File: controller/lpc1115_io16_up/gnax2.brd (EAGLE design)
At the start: 44.5 x 44 mm, 77 parts, among them J2 CON_10-1.27THT, SW1 SWITCH_X, T1 BC547C, T2 BC807-40, U1 DMHC4035LSD, U2 SN74AUP1T32, U3 BD9G101G, U4 LPC1115FBD48/303, U5 M25P10, X1 12MHz, X3 FIDUCIAL_0.6-1.2MM, X8 FIDUCIAL_0.6-1.2MM, X9 FIDUCIAL_0.6-1.2MM

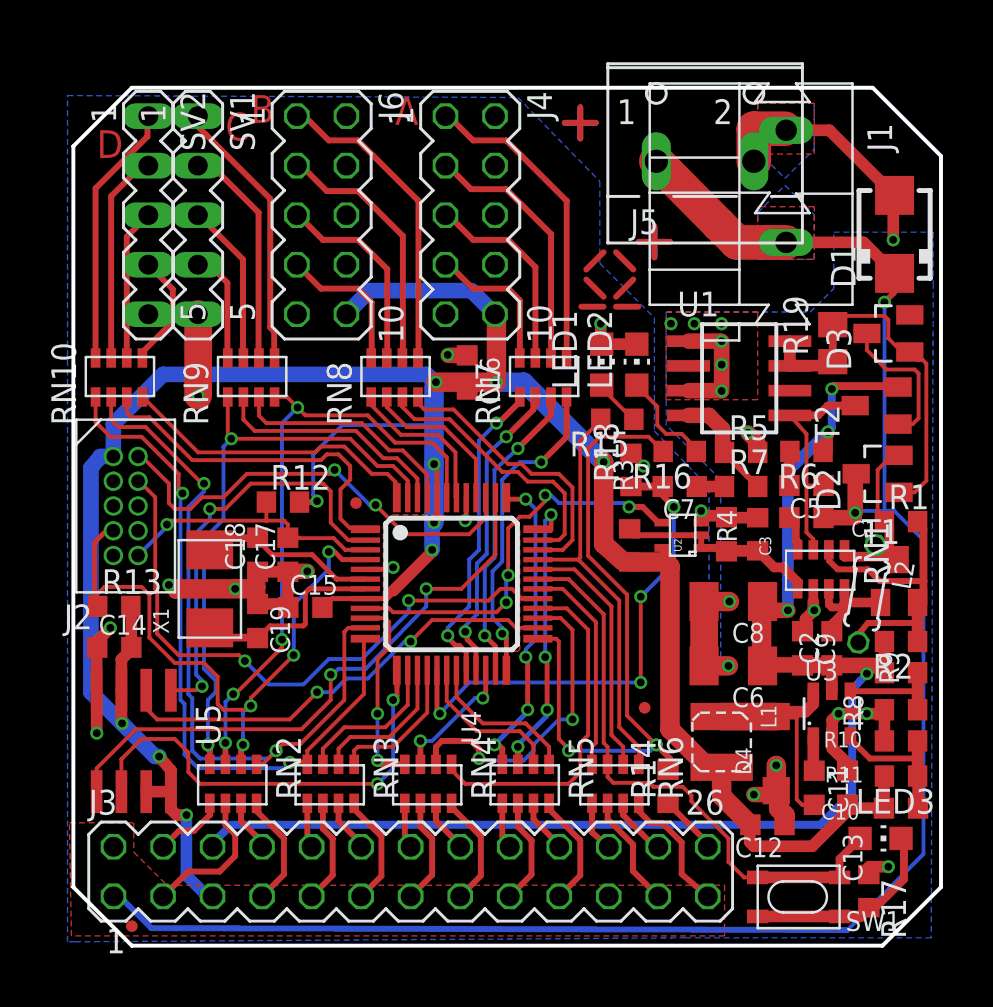
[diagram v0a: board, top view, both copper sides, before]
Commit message: current limiter for transmitter, change prog led behaviour, fix clamp layout
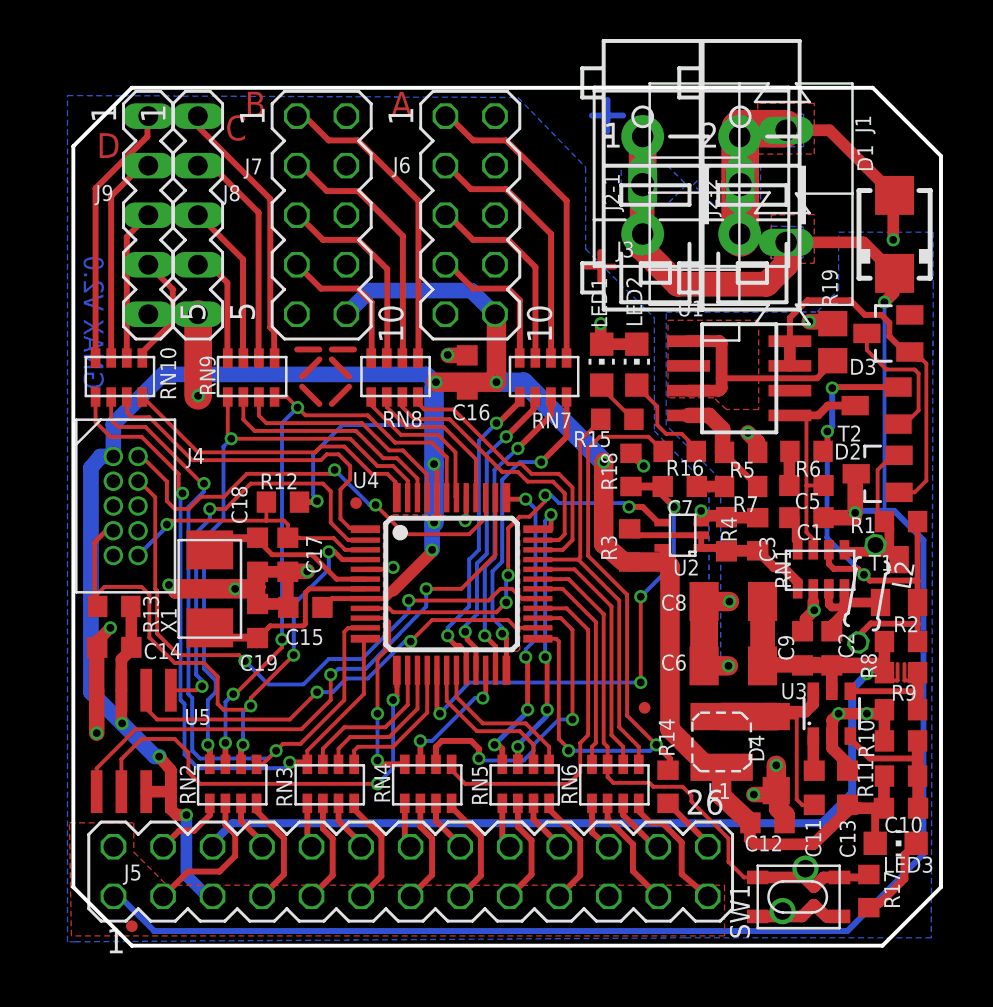
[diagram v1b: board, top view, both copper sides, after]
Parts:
- removed J2: CON_10-1.27THT, 000_ga:CON2X5_127-THT
- added J2-1, J2-2: (no value), con-wago:236-4XX
- added J7: (no value), con-lstb:MA05-2
- C3: value 330p -> 150p
- D3: value 8V2 -> 6V8
- J3: device con-lstb:MA13-2 -> 000_ga:W237-102
- J4: value (none) -> CON_10-1.27THT; device con-lstb:MA05-2 -> 000_ga:CON2X5_127-THT
- J5: device 000_ga:W237-102 -> con-lstb:MA13-2
- R19: value 3R3 -> 2R2
- SW1: value SWITCH_X -> (none)
- moved J5 40.6 mm to (17.3, 3.80)
- moved J3 39.2 mm to (31.7, 40.3)
- moved J4 23.6 mm to (2.05, 22.6)
- moved U$1 15.4 mm to (13.0, 29.0), turned to 180 degrees
- moved J6 7.62 mm to (20.4, 37.5)
- moved LED3 0.81 mm to (42.2, 5.25)
- moved C12 0.10 mm to (35.6, 6.30)
- moved R19 0.05 mm to (39.0, 30.9)
- renumbered SV1 to J8, SV2 to J9
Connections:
- removed net N$40: LED3.C, R17.2, SW1.3, SW1.4
- new net FX: R19.1, U1.1, U1.3
- new net N$46: L2.2, R1.2, R2.1, R6.1, RN1.2, T1.2, T2.E
- net EIB+: now also J2-1.1@1, J2-1.1@2
- net EIB_DC: now also J5.6; no longer J3.6, R6.1, T2.E
- net GND: now also J2-2.1@2, J5.21, J7.2, J7.4, J7.6, J7.8, J7.9, R19.2, SW1.3, SW1.4; no longer J2.9, J3.21, J4.2, J4.4, J4.6, J4.8, R17.1, U1.1, U1.3
- net N$1: no longer R19.1, R19.2
- net N$10: now also J6.5; no longer J4.5
- net N$11: now also J6.3; no longer J4.3
- net N$13: now also J6.1; no longer J4.1
- net N$16: now also J7.5; no longer J6.5
- net N$17: now also J7.3; no longer J6.3
- net N$22: now also J7.7; no longer J6.7
- net N$23: now also J7.1; no longer J6.1
- net N$25: now also LED3.C, R17.2; no longer L2.2, R1.2, R2.1, RN1.2, T1.2
- net N$38: now also J5.3; no longer J3.3
- net N$41: now also J5.7; no longer J3.7
- net N$42: now also J5.9; no longer J3.9
- net N$43: now also J5.11; no longer J3.11
- net N$44: now also J5.13; no longer J3.13
- net N$45: now also J5.4; no longer J3.4
- net N$47: now also J5.8; no longer J3.8
- net N$48: now also J5.10; no longer J3.10
- net N$49: now also J5.12; no longer J3.12
- net N$5: now also J6.7; no longer J4.7
- net N$50: now also J5.14; no longer J3.14
- net N$58: now also J5.15; no longer J3.15
- net N$59: now also J5.17; no longer J3.17
- net N$60: now also J5.16; no longer J3.16
- net N$61: now also J5.18; no longer J3.18
- net N$63: now also J5.19; no longer J3.19
- net N$64: now also J5.20; no longer J3.20
- net N$65: now also J5.22; no longer J3.22
- net N$66: now also J5.23; no longer J3.23
- net N$67: now also J5.24; no longer J3.24
- net N$68: now also J5.25; no longer J3.25
- net N$69: now also J5.26; no longer J3.26
- net RESET: now also J4.10; no longer J2.10
- net SWCLK: now also J4.4; no longer J2.4
- net SWDIO: now also J4.2; no longer J2.2
- net VCC: now also J4.1, J5.5, J7.10, LED3.A; no longer J2.1, J3.5, J4.10
- net XIO23: now also R17.1; no longer LED3.A
- net XIO8/ISP_EN: now also J4.7; no longer J2.7
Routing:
- net N$46: track 0.00 -> 30.4 mm, vias 0 -> 3
- net EIB_DC: track 74.6 -> 57.6 mm, vias 4 -> 1
- net FX: track 0.00 -> 11.9 mm
- net N$25: track 16.3 -> 4.46 mm
- net N$40: track 10.9 -> 0.00 mm
- net GND: track 80.8 -> 89.3 mm, vias 28 -> 23
- net EIB+: track 95.1 -> 102.6 mm
- net VCC: track 141.3 -> 145.1 mm
- net DUMMY3: track 3.20 -> 0.00 mm
- net DUMMY2: track 3.20 -> 0.00 mm
- net N$20: track 5.39 -> 7.31 mm
- net N$12: track 11.8 -> 12.3 mm
- net N$8: track 10.6 -> 10.1 mm
- net XIO23: track 29.9 -> 30.1 mm, vias 0 -> 1
- added copper zone on layer 1, net FX
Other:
- board text added: "GNAX V2.0"

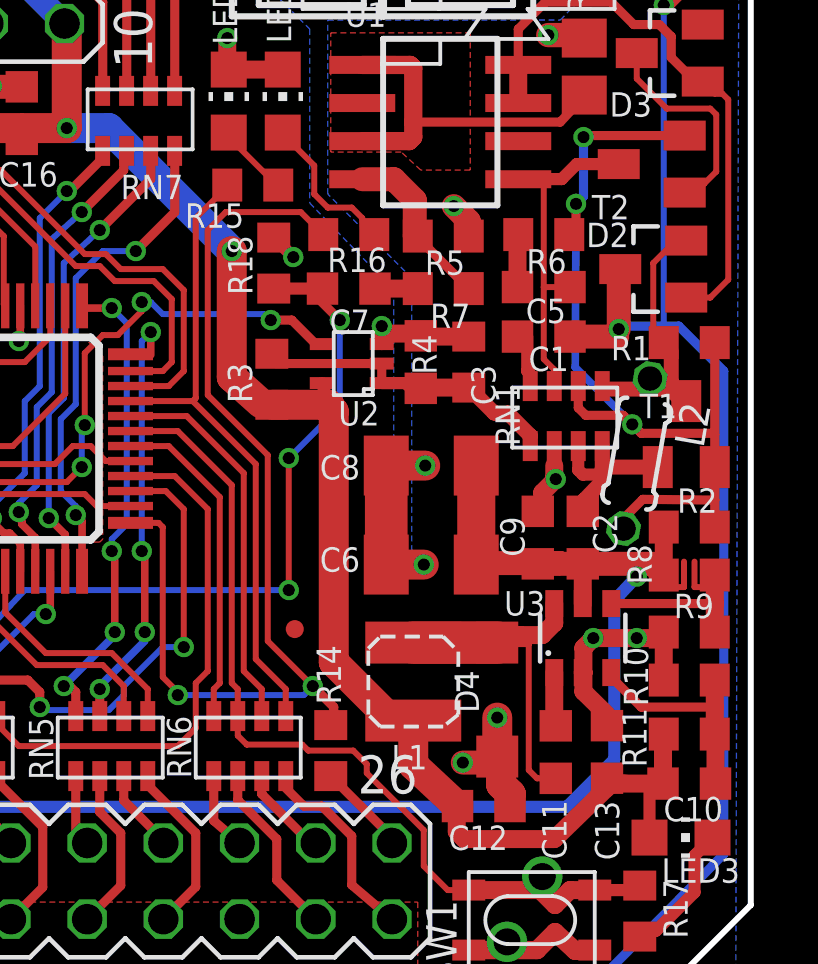
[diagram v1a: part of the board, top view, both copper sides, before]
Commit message: fix receiver voltage protection
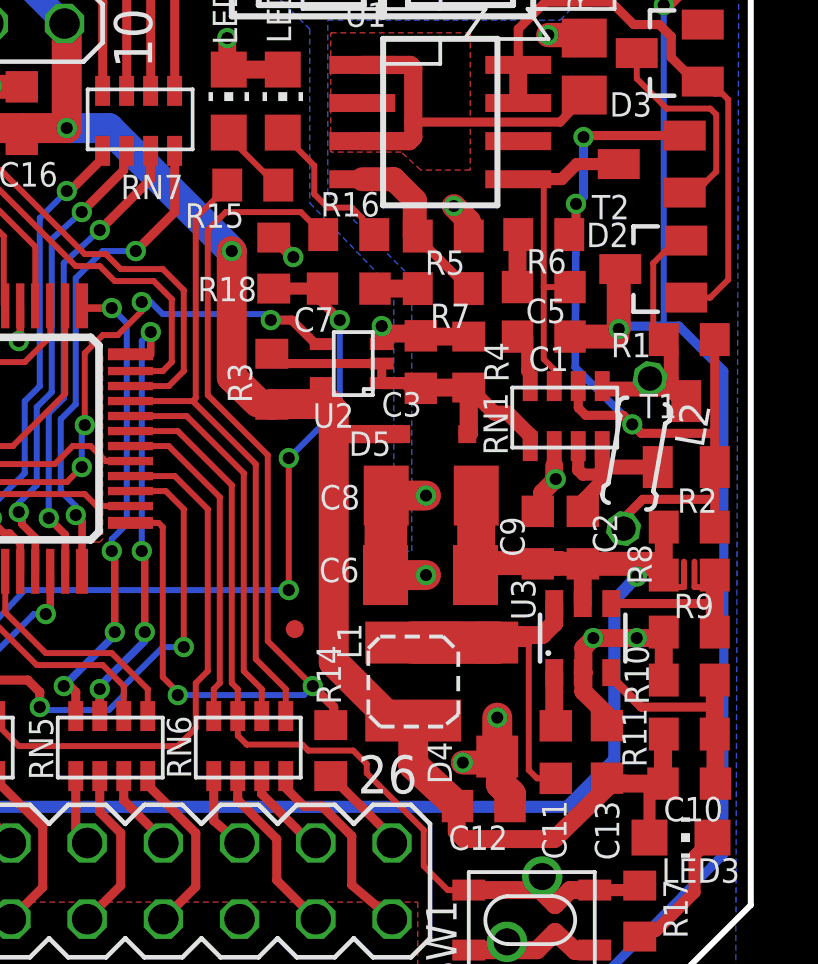
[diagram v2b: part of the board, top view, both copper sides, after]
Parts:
- added D5: 1N4148WX-TP, diode:SOD323-R
- C3: value 150p -> 330p
- moved C8 1.00 mm to (33.9, 16.6)
- moved C6 0.35 mm to (33.8, 14.0)
- moved R1 0.10 mm to (42.5, 21.9)
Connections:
- net N$14: now also D5.A
- net VCC: now also D5.C
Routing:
- net VCC: track 145.1 -> 147.4 mm
- net N$14: track 11.0 -> 12.6 mm
- net EIB_DC: track 57.6 -> 56.9 mm
- net GND: track 89.3 -> 88.8 mm
